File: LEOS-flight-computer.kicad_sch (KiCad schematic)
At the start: 23 parts, among them J1 MicroFit_1x4, J2 MicroFit_1x4, J3 GPIO, J4 I2C Breakout, J5 SPI Breakout, U1 MCP2562FD, U2 MCP2518FD, U3 SAM-M8Q, Y1 40 MHz

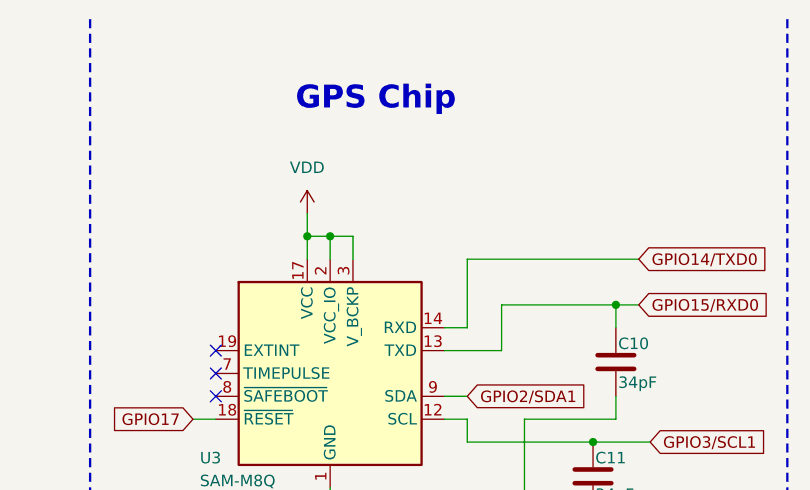
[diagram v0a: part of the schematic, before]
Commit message: Routed and schematiced a coin cell bettery that is connected to V backup on the gps module
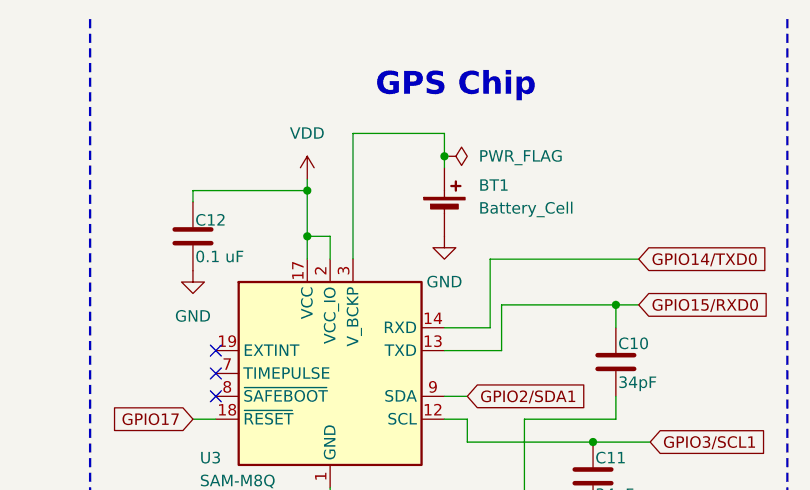
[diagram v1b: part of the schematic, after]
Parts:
- added BT1: Battery_Cell, Battery:BatteryHolder_LINX_BAT-HLD-012-SMT, symbol Device:Battery_Cell
- added C12: 0.1 uF, Capacitor_SMD:C_0603_1608Metric, symbol Device:C
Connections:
- net GND: now also BT1.2 (-), C12.2
- net VDD: now also C12.1; no longer U3.3 (V_BCKP)
- new net: BT1.1 (+), U3.3 (V_BCKP)

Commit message: Update
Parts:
- BT1: value Battery_Cell -> CR2032_Battery_Cell; footprint Battery:BatteryHolder_LINX_BAT-HLD-012-SMT -> CustomFootprints:BatteryHolder_SMD_MYOUNG_BS-08-B2AA010-R
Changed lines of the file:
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@@
 		(on_board yes)
 		(dnp no)
-		(fields_autoplaced yes)
 		(property "Reference" "BT1"
-			(at 157.48 31.1784 0)
+			(at 156.972 31.242 0)
 			(effects
 				(font
@@
 			)
 		)
-		(property "Value" "Battery_Cell"
-			(at 157.48 33.7184 0)
+		(property "Value" "CR2032_Battery_Cell"
+			(at 156.972 34.29 0)
 			(effects
 				(font
@@
 			)
 		)
-		(property "Footprint" "Battery:BatteryHolder_LINX_BAT-HLD-012-SMT"
+		(property "Footprint" "CustomFootprints:BatteryHolder_SMD_MYOUNG_BS-08-B2AA010-R"
 			(at 153.67 32.766 90)
 			(effects

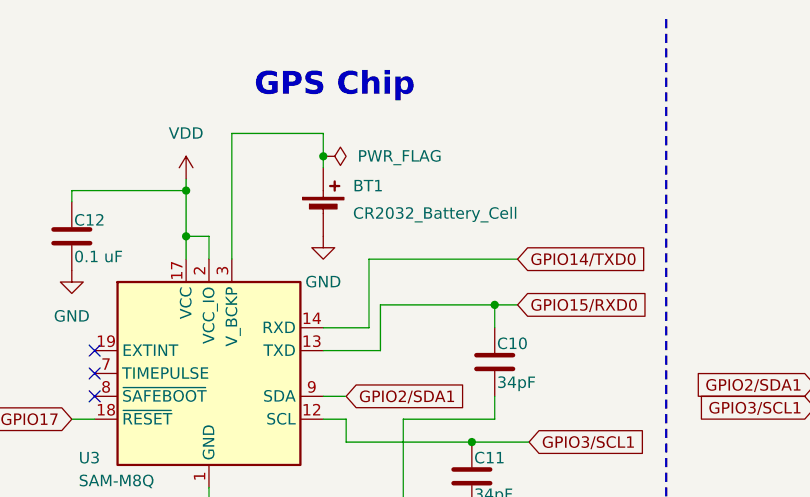
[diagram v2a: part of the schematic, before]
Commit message: changed the battery holder to a better one
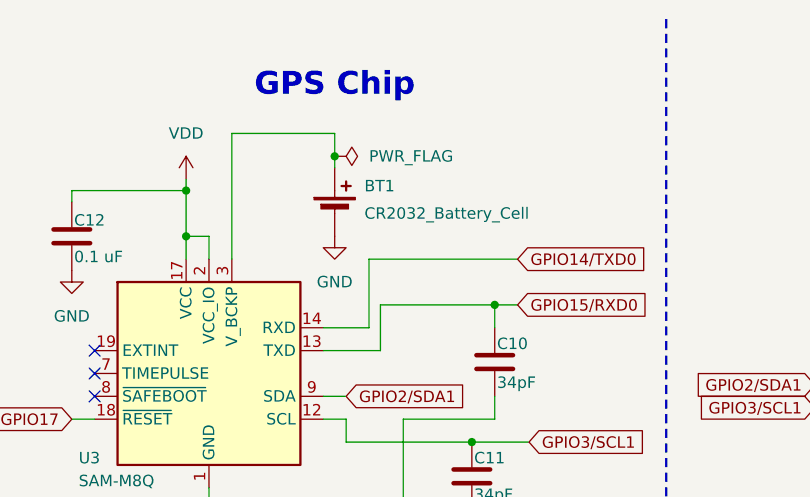
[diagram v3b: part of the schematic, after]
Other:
- moved on the sheet: BT1
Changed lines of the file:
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@@
 	)
 	(junction
-		(at 153.67 27.94)
+		(at 154.94 27.94)
 		(diameter 0)
 		(color 0 0 0 0)
@@
 	(wire
 		(pts
-			(xy 153.67 25.4) (xy 153.67 27.94)
+			(xy 154.94 25.4) (xy 154.94 27.94)
 		)
 		(stroke
@@
 	(wire
 		(pts
-			(xy 153.67 27.94) (xy 153.67 29.21)
+			(xy 154.94 27.94) (xy 154.94 29.21)
 		)
 		(stroke
@@
 	(wire
 		(pts
-			(xy 143.51 25.4) (xy 153.67 25.4)
+			(xy 143.51 25.4) (xy 154.94 25.4)
 		)
 		(stroke
@@
 	(symbol
 		(lib_id "Device:Battery_Cell")
-		(at 153.67 34.29 0)
+		(at 154.94 34.29 0)
 		(unit 1)
 		(exclude_from_sim no)
@@
 		(dnp no)
 		(property "Reference" "BT1"
-			(at 156.972 31.242 0)
+			(at 158.242 31.242 0)
 			(effects
 				(font
@@
 		)
 		(property "Value" "CR2032_Battery_Cell"
-			(at 156.972 34.29 0)
+			(at 158.242 34.29 0)
 			(effects
 				(font
@@
 		)
 		(property "Footprint" "CustomFootprints:BatteryHolder_SMD_MYOUNG_BS-08-B2AA010-R"
-			(at 153.67 32.766 90)
+			(at 154.94 32.766 90)
 			(effects
 				(font
@@
 		)
 		(property "Datasheet" "~"
-			(at 153.67 32.766 90)
+			(at 154.94 32.766 90)
 			(effects
 				(font
@@
 		)
 		(property "Description" "Single-cell battery"
-			(at 153.67 34.29 0)
+			(at 154.94 34.29 0)
 			(effects
 				(font
@@
 	(symbol
 		(lib_id "power:PWR_FLAG")
-		(at 153.67 27.94 270)
+		(at 154.94 27.94 270)
 		(unit 1)
 		(exclude_from_sim no)
@@
 		(fields_autoplaced yes)
 		(property "Reference" "#FLG04"
-			(at 155.575 27.94 0)
+			(at 156.845 27.94 0)
 			(effects
 				(font
@@
 		)
 		(property "Value" "PWR_FLAG"
-			(at 157.48 27.9399 90)
+			(at 158.75 27.9399 90)
 			(effects
 				(font
@@
 		)
 		(property "Footprint" ""
-			(at 153.67 27.94 0)
+			(at 154.94 27.94 0)
 			(effects
 				(font
@@
 		)
 		(property "Datasheet" "~"
-			(at 153.67 27.94 0)
+			(at 154.94 27.94 0)
 			(effects
 				(font
@@
 		)
 		(property "Description" "Special symbol for telling ERC where power comes from"
-			(at 153.67 27.94 0)
+			(at 154.94 27.94 0)
 			(effects
 				(font
@@
 	(symbol
 		(lib_id "power:GND")
-		(at 153.67 36.83 0)
+		(at 154.94 36.83 0)
 		(unit 1)
 		(exclude_from_sim no)
@@
 		(fields_autoplaced yes)
 		(property "Reference" "#PWR025"
-			(at 153.67 43.18 0)
+			(at 154.94 43.18 0)
 			(effects
 				(font
@@
 		)
 		(property "Value" "GND"
-			(at 153.67 41.91 0)
+			(at 154.94 41.91 0)
 			(effects
 				(font
@@
 		)
 		(property "Footprint" ""
-			(at 153.67 36.83 0)
+			(at 154.94 36.83 0)
 			(effects
 				(font
@@
 		)
 		(property "Datasheet" ""
-			(at 153.67 36.83 0)
+			(at 154.94 36.83 0)
 			(effects
 				(font
@@
 		)
 		(property "Description" "Power symbol creates a global label with name \"GND\" , ground"
-			(at 153.67 36.83 0)
-			(effects
-				(font
+			(at 154.94 36.83 0)
+			(effects
+				(font

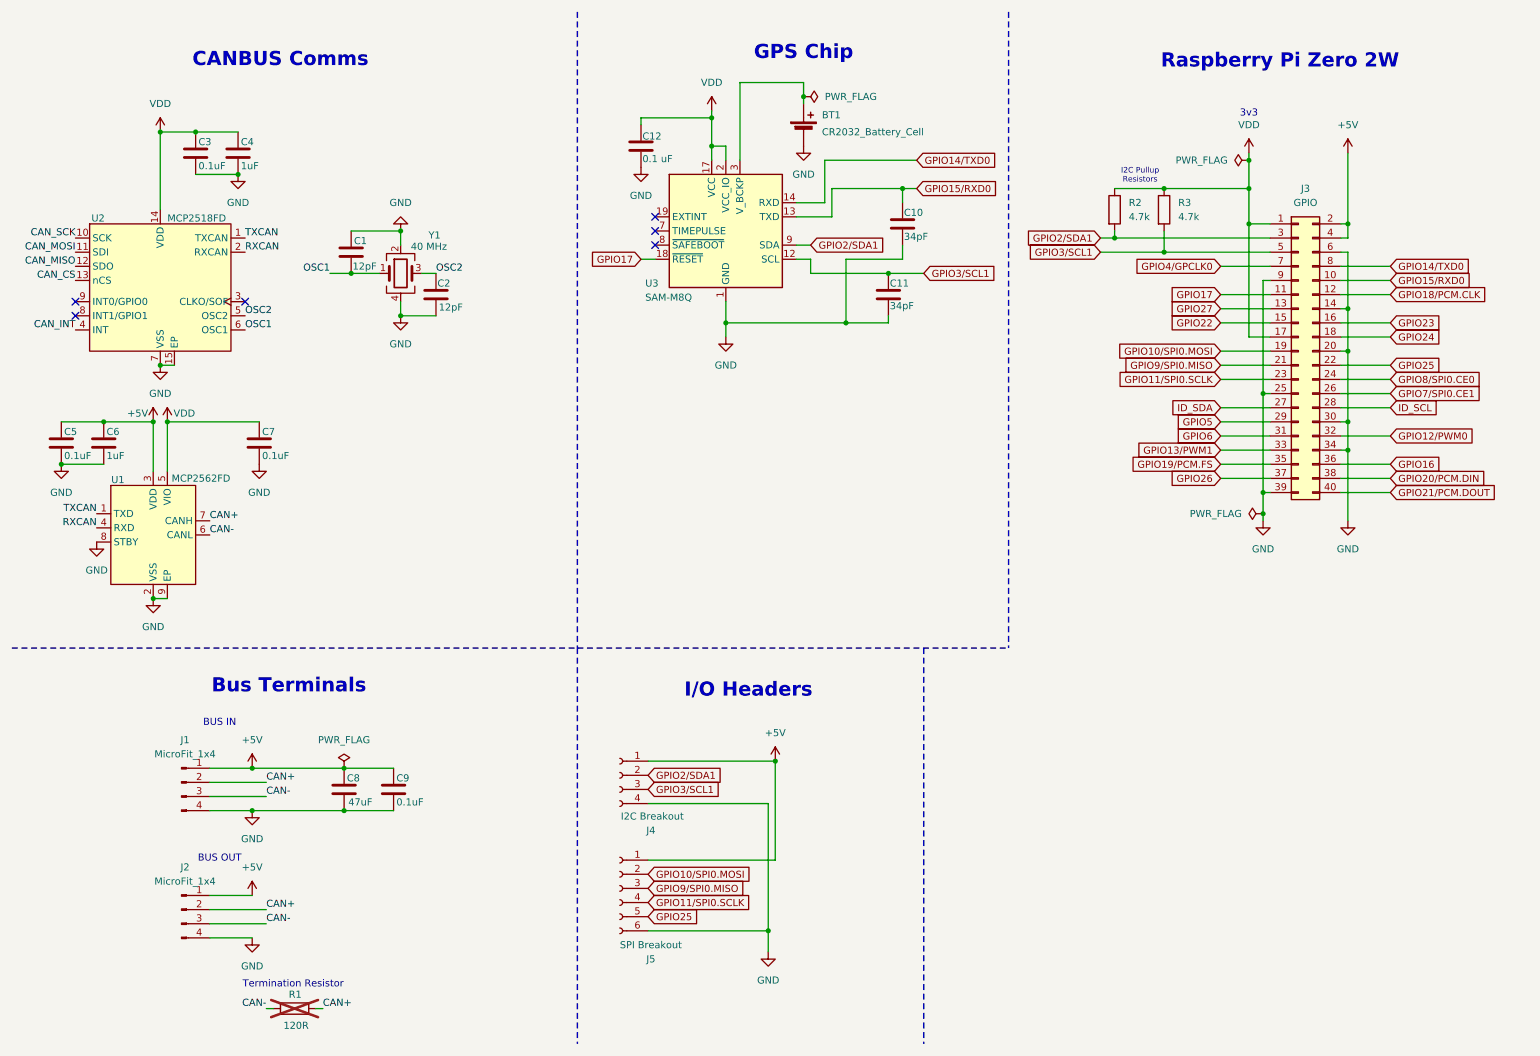
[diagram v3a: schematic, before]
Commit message: Added labels and CANBus SPI connections
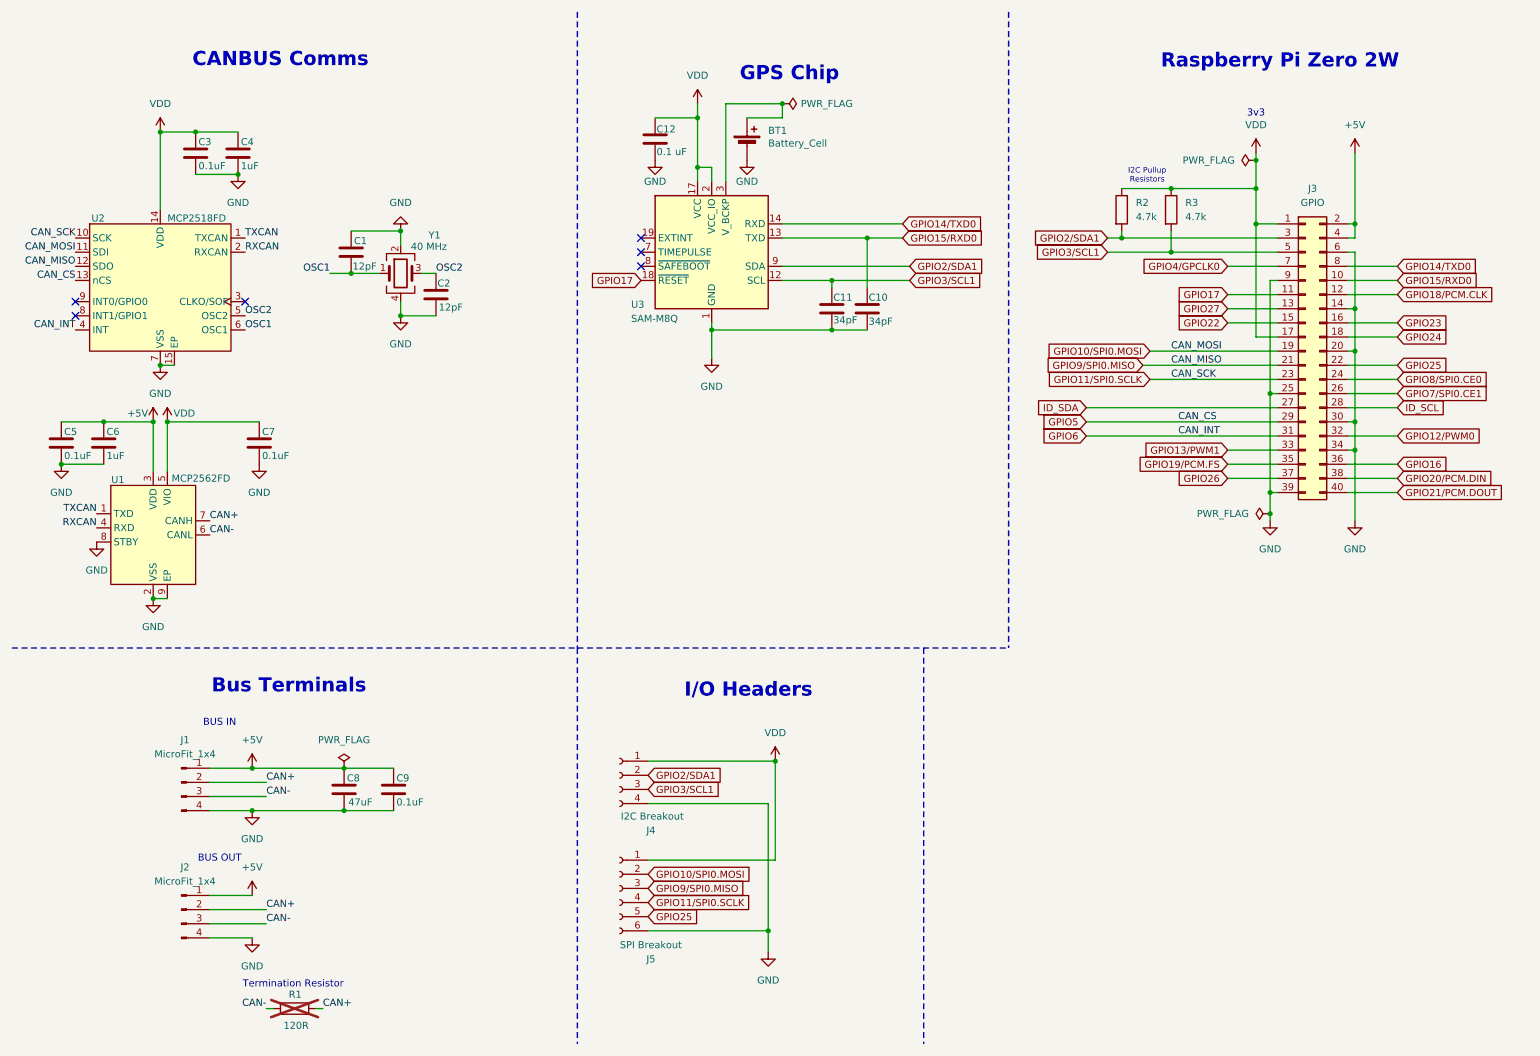
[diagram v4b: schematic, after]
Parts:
- BT1: value CR2032_Battery_Cell -> Battery_Cell
- C1, C2, C3, C4, C5, C6, C7, C8, C9: footprint Capacitor_SMD:C_0201_0603Metric -> Capacitor_SMD:C_0603_1608Metric
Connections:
- net CAN_CS is gone; now on net GPIO5: U2.13 (nCS)
- net CAN_INT is gone; now on net GPIO6: U2.4 (INT)
- net CAN_MISO is gone; now on net GPIO9/SPI0.MISO: U2.12 (SDO)
- net CAN_MOSI is gone; now on net GPIO10/SPI0.MOSI: U2.11 (SDI)
- net CAN_SCK is gone; now on net GPIO11/SPI0.SCLK: U2.10 (SCK)
- net +5V: no longer J4.1 (Pin_1), J5.1 (Pin_1)
- net VDD: now also J4.1 (Pin_1), J5.1 (Pin_1)
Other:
- moved on the sheet: BT1, C10, C11, C12, J3, R2, R3, U3

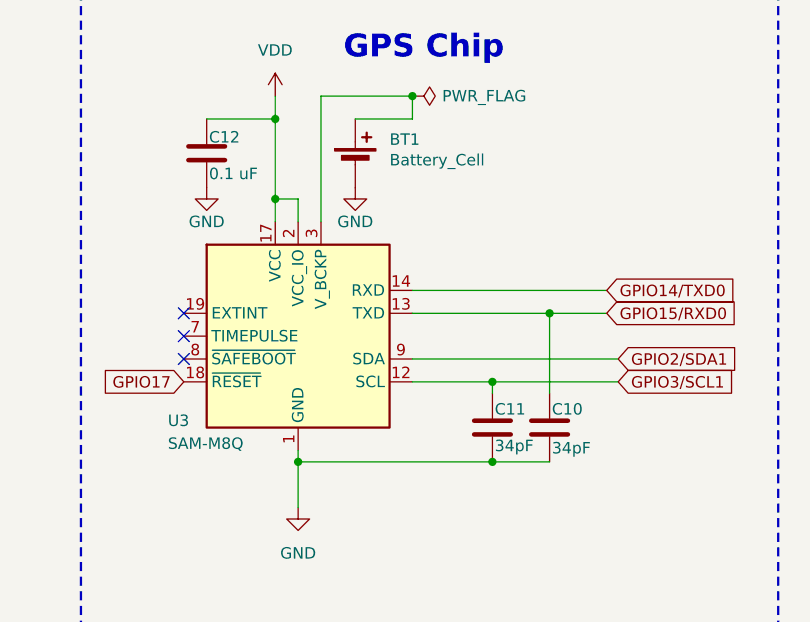
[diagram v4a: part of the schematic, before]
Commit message: Added part numbers
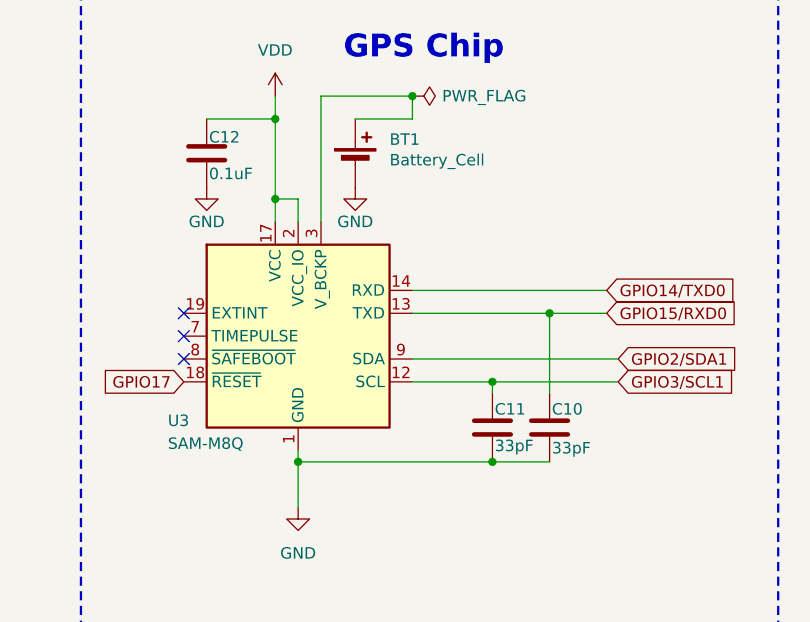
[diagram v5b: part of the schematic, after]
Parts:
- C1, C2: MPN (none) -> GRM0335C1E120JA01D; Manufacturer (none) -> Murata
- C10, C11: value 34pF -> 33pF; MPN (none) -> GRM1885C1H330JA01D; Manufacturer (none) -> Murata
- C12: value 0.1 uF -> 0.1uF; MPN (none) -> GRM033C71C104KE14D; Manufacturer (none) -> Murata
- C3, C5, C7, C9: MPN (none) -> GRM033C71C104KE14D; Manufacturer (none) -> Murata
- C4, C6: MPN (none) -> GRT033R60J105ME13D; Manufacturer (none) -> Murata
- C8: MPN (none) -> GRM033R60J474KE90D; Manufacturer (none) -> Murata
- J1, J2: MPN (none) -> 43650-0411; Manufacturer (none) -> Molex
- U1: MPN (none) -> MCP2562FDT-H/SN; Manufacturer (none) -> Microchip
- U2: MPN (none) -> MCP2518FDT-E/SL; Manufacturer (none) -> Microchip

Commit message: Added manufacturers and MPNs for the parts
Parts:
- BT1: MPN (none) -> BS-08-B2AA010-R; Manufacturer (none) -> MYOUNG
- J4: MPN (none) -> PPTC041LGBN-RC; Manufacturer (none) -> Sullins Connectors
- J5: MPN (none) -> PPTC061LGBN-RC; Manufacturer (none) -> Sullins Connectors
- R2, R3: MPN (none) -> MCT06030C4701FP500; Manufacturer (none) -> Vishay
- U3: MPN (none) -> SAM-M8Q-0; Manufacturer (none) -> u-blox
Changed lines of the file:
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@@
 			)
 		)
+		(property "MPN" "BS-08-B2AA010-R"
+			(at 144.78 36.83 0)
+			(effects
+				(font
+					(size 1.27 1.27)
+				)
+				(hide yes)
+			)
+		)
+		(property "Manufacturer" "MYOUNG"
+			(at 144.78 36.83 0)
+			(effects
+				(font
+					(size 1.27 1.27)
+				)
+				(hide yes)
+			)
+		)
 		(pin "2"
 		)
@@
 			)
 		)
+		(property "MPN" "  PPTC061LGBN-RC"
+			(at 121.92 170.18 0)
+			(effects
+				(font
+					(size 1.27 1.27)
+				)
+				(hide yes)
+			)
+		)
+		(property "Manufacturer" "Sullins Connectors"
+			(at 121.92 170.18 0)
+			(effects
+				(font
+					(size 1.27 1.27)
+				)
+				(hide yes)
+			)
+		)
 		(pin "3"
 		)
@@
 			)
 		)
+		(property "MPN" "MCT06030C4701FP500"
+			(at 220.98 48.26 0)
+			(effects
+				(font
+					(size 1.27 1.27)
+				)
+				(hide yes)
+			)
+		)
+		(property "Manufacturer" "Vishay"
+			(at 220.98 48.26 0)
+			(effects
+				(font
+					(size 1.27 1.27)
+				)
+				(hide yes)
+			)
+		)
 		(pin "2"
 		)
@@
 			)
 		)
+		(property "MPN" "MCT06030C4701FP500"
+			(at 212.09 48.26 0)
+			(effects
+				(font
+					(size 1.27 1.27)
+				)
+				(hide yes)
+			)
+		)
+		(property "Manufacturer" "Vishay"
+			(at 212.09 48.26 0)
+			(effects
+				(font
+					(size 1.27 1.27)
+				)
+				(hide yes)
+			)
+		)
 		(pin "2"
 		)
@@
 			)
 		)
+		(property "MPN" "SAM-M8Q-0"
+			(at 138.43 55.88 0)
+			(effects
+				(font
+					(size 1.27 1.27)
+				)
+				(hide yes)
+			)
+		)
+		(property "Manufacturer" "u-blox"
+			(at 138.43 55.88 0)
+			(effects
+				(font
+					(size 1.27 1.27)
+				)
+				(hide yes)
+			)
+		)
 		(pin "19"
 		)
@@
 			(at 121.92 149.86 0)
 			(effects
+				(font
+					(size 1.27 1.27)
+				)
+				(hide yes)
+			)
+		)
+		(property "MPN" "  PPTC041LGBN-RC"
+			(at 121.92 149.86 0)
+			(effects
+				(font
+					(size 1.27 1.27)
+				)
+				(hide yes)
+			)
+		)
+		(property "Manufacturer" "Sullins Connectors"
+			(at 121.92 149.86 0)
+			(effects

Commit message: Final updates before production - Includes GARY.
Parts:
- C1, C2: value 12pF -> 18pF; MPN GRM0335C1E120JA01D -> GRM1885C1H180GA01D
- C4, C6: MPN GRT033R60J105ME13D -> GRM188C81E105KAADD
- J3, R1: now left out of the parts list
- U1: MPN MCP2562FDT-H/SN -> MCP2562FDT-H/SN
- U2: MPN MCP2518FDT-E/SL -> MCP2518FDT-E/SL
- Y1: MPN (none) -> ECS-400-12-33Q-JEN-TR; Manufacturer (none) -> ECS
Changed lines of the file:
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@@
 		(unit 1)
 		(exclude_from_sim no)
-		(in_bom yes)
+		(in_bom no)
 		(on_board yes)
 		(dnp no)
@@
 			)
 		)
-		(property "Value" "12pF"
+		(property "Value" "18pF"
 			(at 89.408 65.786 0)
 			(effects
@@
 			)
 		)
-		(property "MPN" "GRM0335C1E120JA01D"
+		(property "MPN" "GRM1885C1H180GA01D"
 			(at 88.9 63.5 0)
 			(effects
@@
 			)
 		)
-		(property "MPN" "GRT033R60J105ME13D"
+		(property "MPN" "GRM188C81E105KAADD"
 			(at 29.21 90.17 0)
 			(effects
@@
 			)
 		)
-		(property "MPN" "GRT033R60J105ME13D"
+		(property "MPN" "GRM188C81E105KAADD"
 			(at 53.34 38.1 0)
 			(effects
@@
 			)
 		)
-		(property "Value" "12pF"
+		(property "Value" "18pF"
 			(at 73.914 58.42 0)
 			(effects
@@
 			)
 		)
-		(property "MPN" "GRM0335C1E120JA01D"
+		(property "MPN" "GRM1885C1H180GA01D"
 			(at 73.66 55.88 0)
 			(effects
@@
 			)
 		)
-		(property "MPN" "  MCP2562FDT-H/SN"
+		(property "MPN" "MCP2562FDT-H/SN"
 			(at 38.1 106.68 0)
 			(effects
@@
 		(unit 1)
 		(exclude_from_sim no)
-		(in_bom yes)
+		(in_bom no)
 		(on_board yes)
 		(dnp yes)
@@
 			)
 		)
-		(property "MPN" " MCP2518FDT-E/SL"
+		(property "MPN" "MCP2518FDT-E/SL"
 			(at 39.37 60.96 0)
 			(effects
@@
 			(at 82.55 59.69 0)
 			(effects
+				(font
+					(size 1.27 1.27)
+				)
+				(hide yes)
+			)
+		)
+		(property "MPN" "ECS-400-12-33Q-JEN-TR "
+			(at 82.55 59.69 0)
+			(effects
+				(font
+					(size 1.27 1.27)
+				)
+				(hide yes)
+			)
+		)
+		(property "Manufacturer" "ECS"
+			(at 82.55 59.69 0)
+			(effects
